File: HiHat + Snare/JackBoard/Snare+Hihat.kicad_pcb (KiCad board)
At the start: 2 copper layers, 40 x 110 mm, 36 parts, among them J1 Snare IN, J10 Conn_01x03_Female, J3 HiHat IN, J4 Snare OUT, J6 Conn_01x08_Female, J8 Conn_01x08_Female, J9 HiHat OUT, Q4 2N3904, Q8 2N3904, U1 TL072

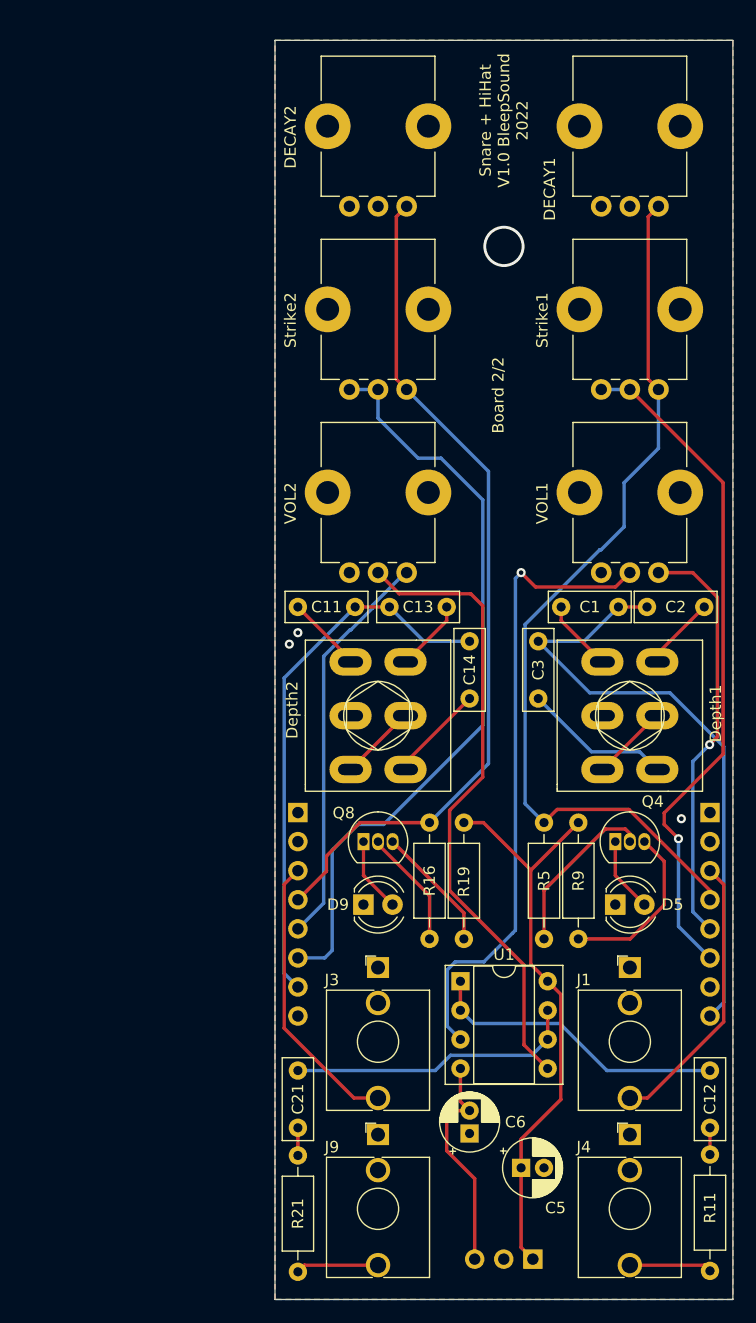
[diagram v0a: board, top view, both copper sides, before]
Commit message: Update front panel and jack board for better handling
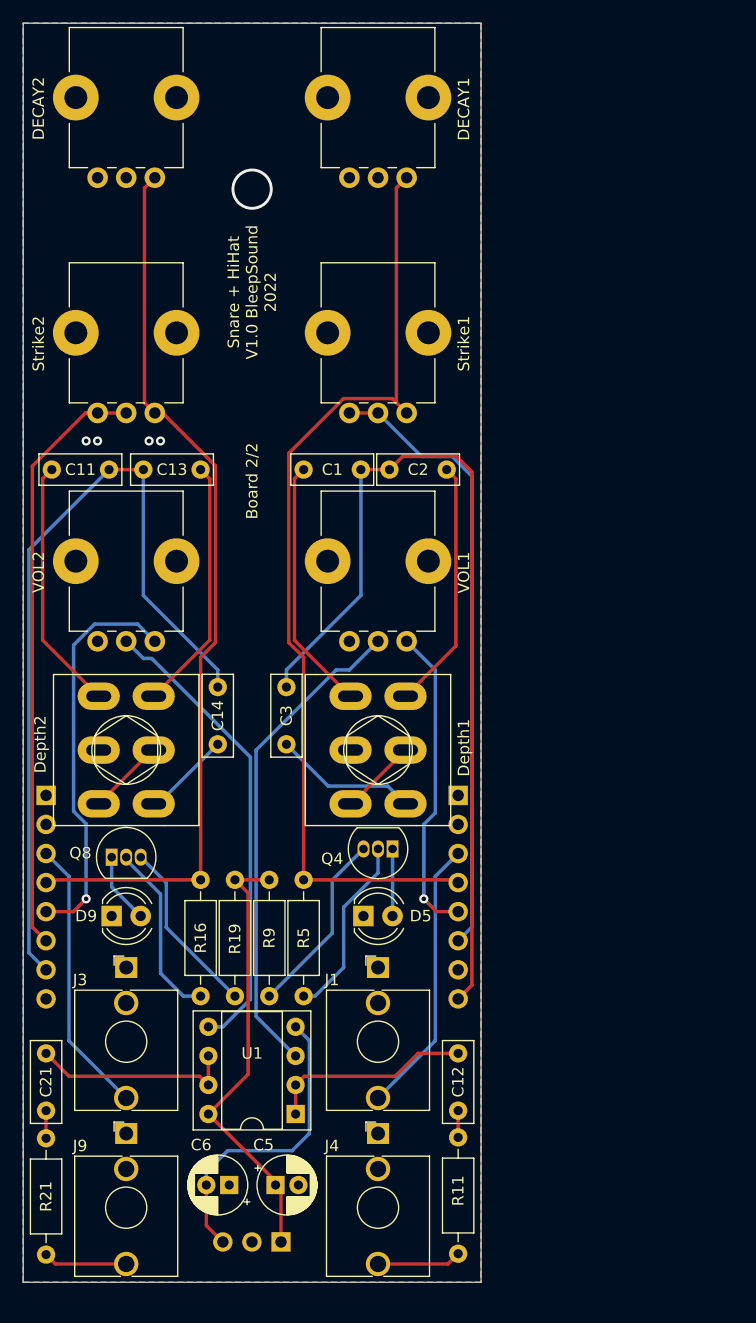
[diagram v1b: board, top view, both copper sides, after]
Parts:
- moved R9 27.5 mm to (72.5, 104.3)
- moved C1 25.5 mm to (80.5, 68.5)
- moved C2 25.5 mm to (83.0, 68.5)
- moved C11 24.6 mm to (58.5, 68.5)
- moved C13 24.6 mm to (61.5, 68.5)
- moved VOL1 22.8 mm to (84.5, 83.5)
- moved VOL2 22.8 mm to (62.5, 83.5)
- moved C14 22.4 mm to (68.0, 87.5)
- moved C3 22.4 mm to (74.0, 87.5)
- moved Depth1 22.2 mm to (82.0, 93.0)
- moved Depth2 22.2 mm to (60.0, 93.0)
- moved DECAY1 22.1 mm to (84.5, 43.0)
- moved DECAY2 22.1 mm to (62.5, 43.0)
- moved Strike1 22.1 mm to (84.5, 63.5)
- moved Strike2 22.1 mm to (62.5, 63.5)
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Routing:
- net /HiDH: track 47.5 -> 71.9 mm
- net /DeH: track 54.8 -> 79.0 mm
- net Net-(C13-Pad2): track 6.29 -> 22.2 mm
- net Net-(C1-Pad2): track 6.29 -> 22.2 mm
- net Net-(C11-Pad2): track 6.71 -> 22.2 mm
- net Net-(C2-Pad2): track 6.50 -> 22.0 mm
- net Net-(VOL2-Pad2): track 55.5 -> 40.9 mm
- net /Ho: track 66.5 -> 52.1 mm
- net Net-(VOL1-Pad2): track 55.9 -> 43.4 mm, vias 1 -> 0
- net +12V: track 50.4 -> 39.2 mm
- net /SnO: track 36.5 -> 27.4 mm
- net Net-(U1-Pad2): track 26.5 -> 17.9 mm
- net -12V: track 19.5 -> 27.2 mm
- net Net-(C21-Pad1): track 25.5 -> 17.9 mm
- net Net-(Q8-Pad2): track 10.4 -> 15.7 mm
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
